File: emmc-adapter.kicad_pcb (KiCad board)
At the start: 2 copper layers, 20 x 31.5 mm, 8 parts, among them J1 Micro_SD_Card, U1 THGBMNG5D1LBAIL

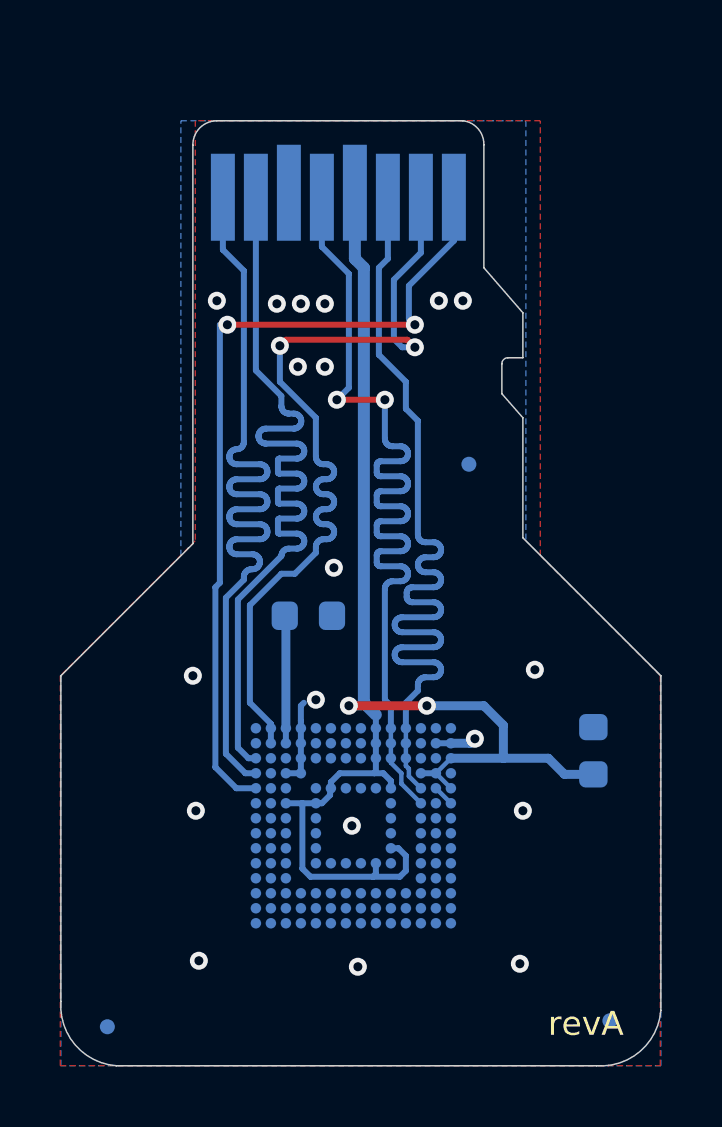
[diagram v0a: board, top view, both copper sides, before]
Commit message: Project updated to Kicad v8
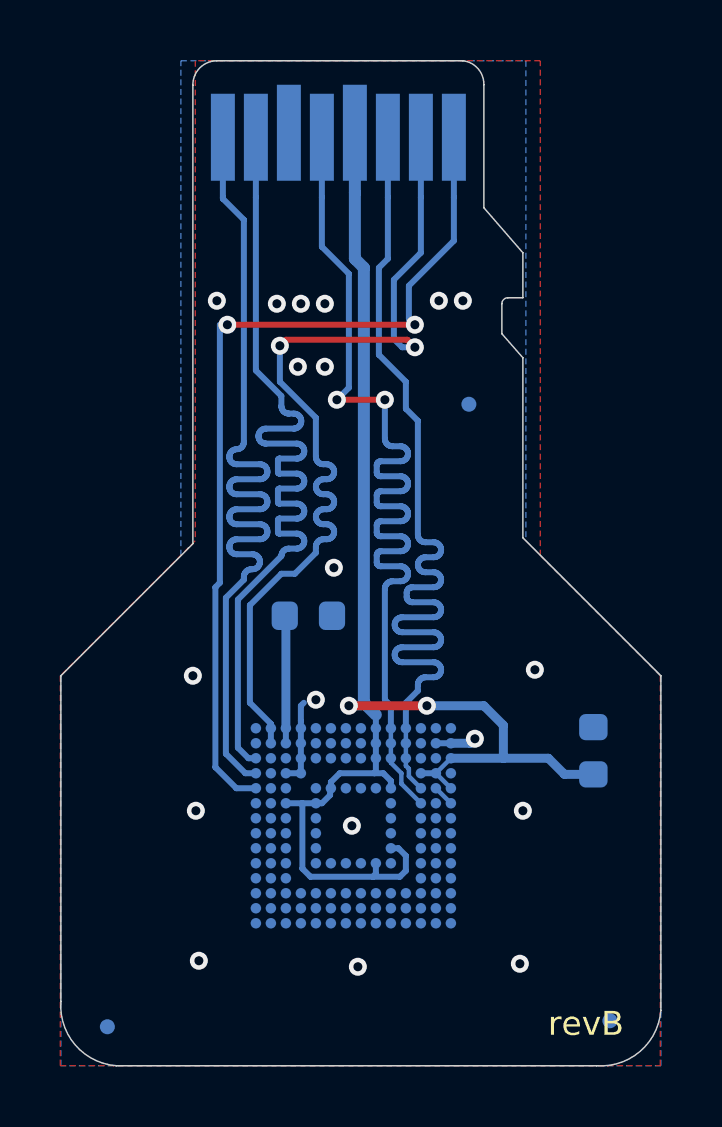
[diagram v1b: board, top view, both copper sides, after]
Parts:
- moved FID3 2.00 mm to (122.6, 60.5)
- moved J1 2.00 mm to (118.2, 57.8)
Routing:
- net /CMD: track 30.2 -> 32.2 mm
- net VCC: track 45.5 -> 47.5 mm
- net /DAT3: track 28.2 -> 30.2 mm
- net /DAT2: track 27.9 -> 29.9 mm
- net /DAT1: track 28.1 -> 30.1 mm
- net /CLK: track 31.0 -> 33.0 mm
- net /DAT0: track 28.0 -> 30.0 mm
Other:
- board size 20 x 31.5 mm -> 20 x 33.5 mm
- net class Default removed
- board text added: "revB"
- board text removed: "revA"
